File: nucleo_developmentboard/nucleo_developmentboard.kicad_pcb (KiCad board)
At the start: 2 copper layers, 65.2 x 82.4 mm, 26 parts, among them J3 Conn_01x02_Socket, J4 MOTOR2 OUT, J5 Conn_PinHeader_1x05_P2.54mm_V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, J6 MOTOR2 OUT, U1 NUCLEO-L432KC, U2 L293D, U3 LM7805_soic, U4 HM-11_Module

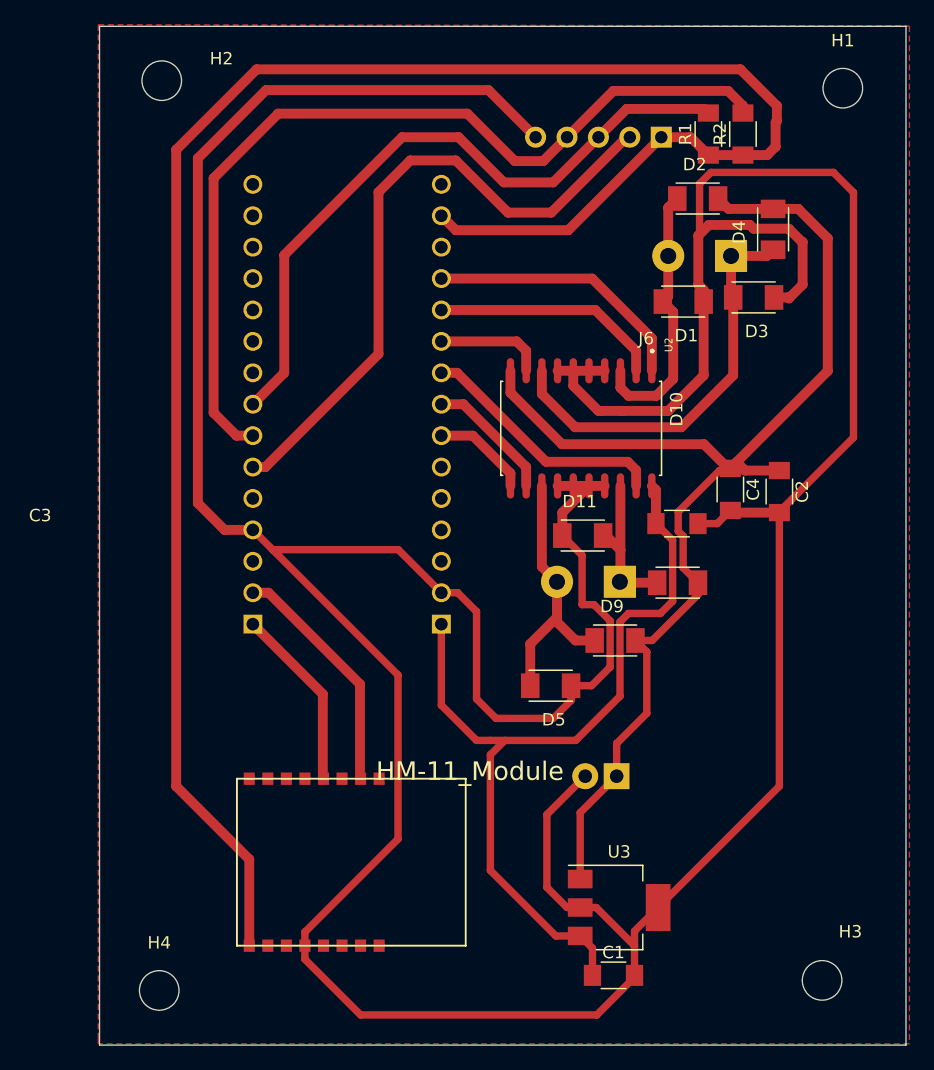
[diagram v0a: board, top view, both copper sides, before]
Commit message: added LSM303CTR
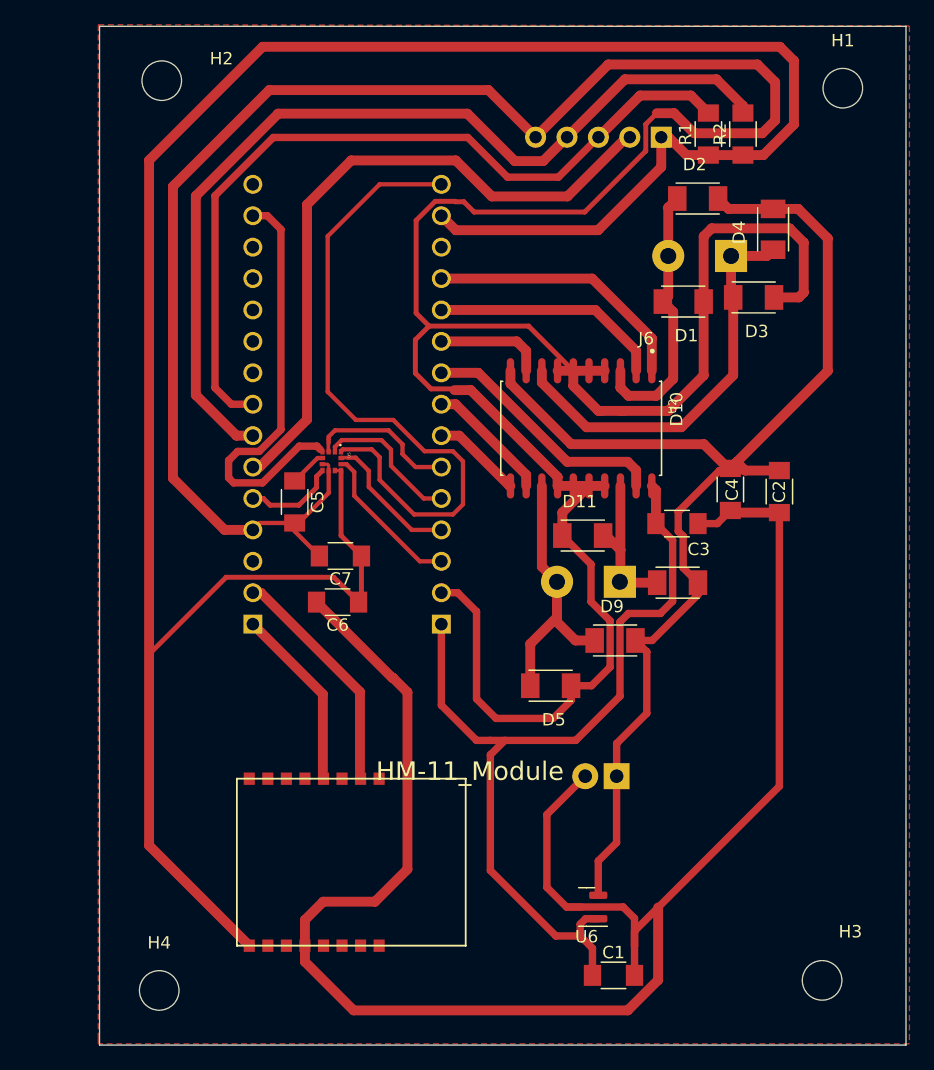
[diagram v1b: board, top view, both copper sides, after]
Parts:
- removed U3: LM7805_soic, fab:SOT-223-3_TabPin2
- added C5: 100nF, fab:C_1206, F.Cu at (201.5, 84.1)
- added C6: 100nF, fab:C_1206, F.Cu at (205.0, 92.2)
- added C7: 10uF, fab:C_1206, F.Cu at (205.2, 88.5)
- added U5: LSM303CTR, LSM303CTR:LGA12R50P_200X200X100, F.Cu at (204.5, 80.8)
- added U6: LM3480-5.0, Package_TO_SOT_SMD:SOT-23, F.Cu at (225.1, 116.8)
- C1: value C_Polarized -> 10uF
- C2, C3, C4: value C_Polarized_Small -> 10uF
- J5: value Conn_PinHeader_1x05_P2.54mm_Vertical_THT_D1mm -> LIDAR_conn
- R1: value 10k -> 1k
- R2: value 10k -> 1K
- U2: value L293D -> L293DD
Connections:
- U1 pad CN3_14: unconnected-(U1A-PB5-PadCN3_14) -> SDOI
- U1 pad CN3_5: unconnected-(U1A-PA12-PadCN3_5) -> INT_MAG
- U1 pad CN4_15: unconnected-(U1B-PB3-PadCN4_15) -> SCLK
- U1 pad CN4_3: unconnected-(U1B-NRST_CN4-PadCN4_3) -> DRDY
- U1 pad CN4_4: unconnected-(U1B-+5V-PadCN4_4) -> INT_XL
- U1 pad CN4_5: unconnected-(U1B-PA2-PadCN4_5) -> SXL
- U1 pad CN4_6: unconnected-(U1B-PA7-PadCN4_6) -> SMAG
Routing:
- net 3V3: track 154.1 -> 222.5 mm
- net GND: track 357.8 -> 417.8 mm
- net SCLK: track 0.00 -> 53.8 mm
- net SDOI: track 0.00 -> 34.5 mm
- net SMAG: track 0.00 -> 12.6 mm
- net DRDY: track 0.00 -> 12.2 mm
- net SXL: track 0.00 -> 11.6 mm
- net INT_XL: track 0.00 -> 11.3 mm
- net SCL: track 55.5 -> 65.6 mm
- net INT_MAG: track 0.00 -> 7.43 mm
- net Net-(U5-C1): track 0.00 -> 3.01 mm
- net VCC: track 68.7 -> 71.3 mm
- net SDA: track 72.9 -> 74.9 mm
- net XSHUT: track 52.7 -> 54.1 mm
- net EN_B: track 7.87 -> 7.27 mm
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
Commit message: Added polarities to components
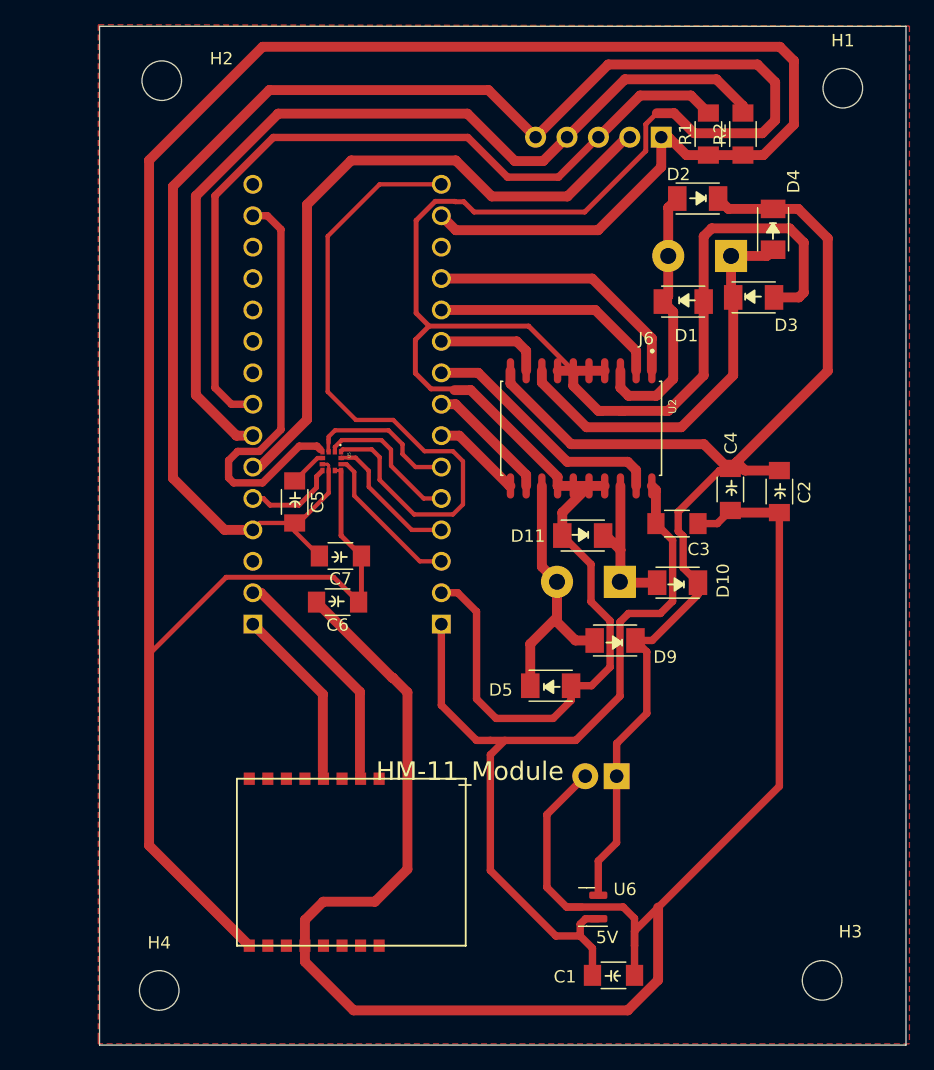
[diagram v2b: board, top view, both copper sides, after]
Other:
- board text added: "+3V"
- board text added: "+BAT"
- board text added: "5V"
